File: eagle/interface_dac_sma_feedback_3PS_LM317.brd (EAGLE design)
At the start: 95.6 x 144.9 mm, 38 parts, among them IC1 ISO1540, X1 BU-SMA-V

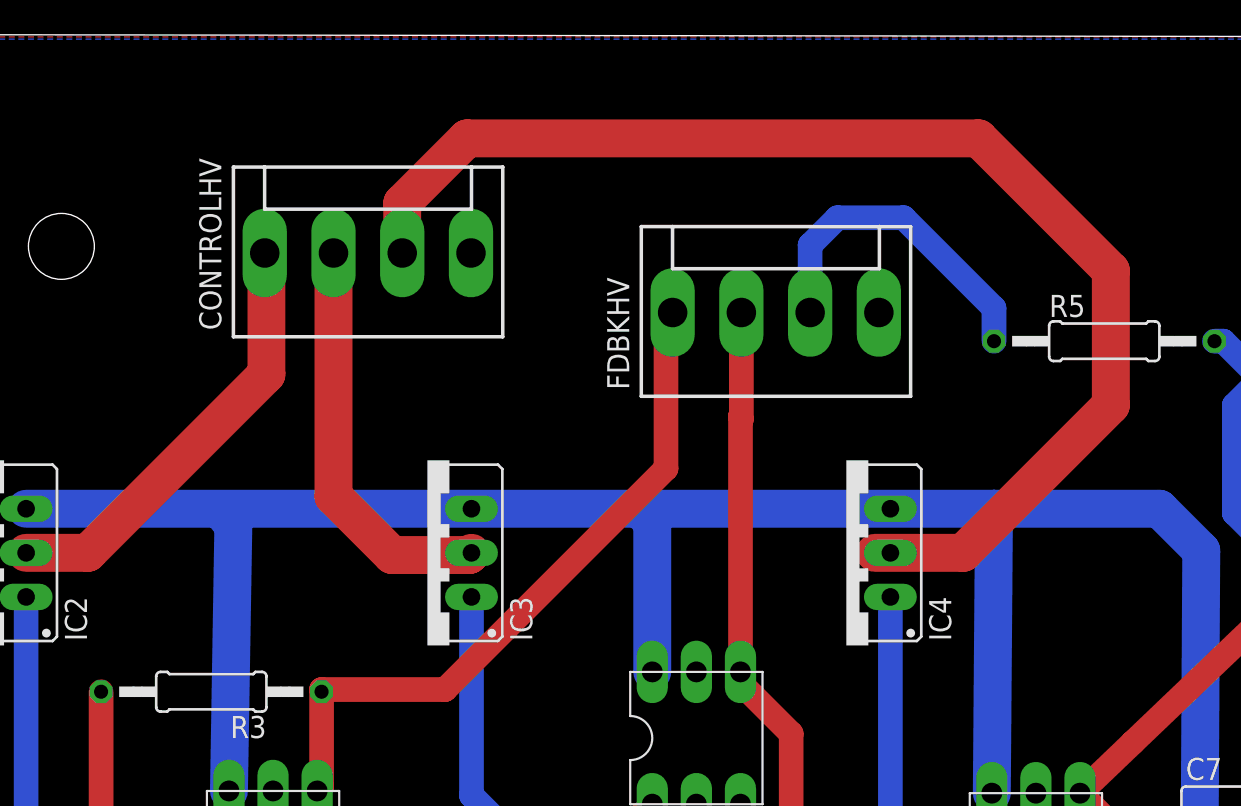
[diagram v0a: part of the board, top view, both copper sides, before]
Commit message: ultra layout. try that next time with lm317 interface
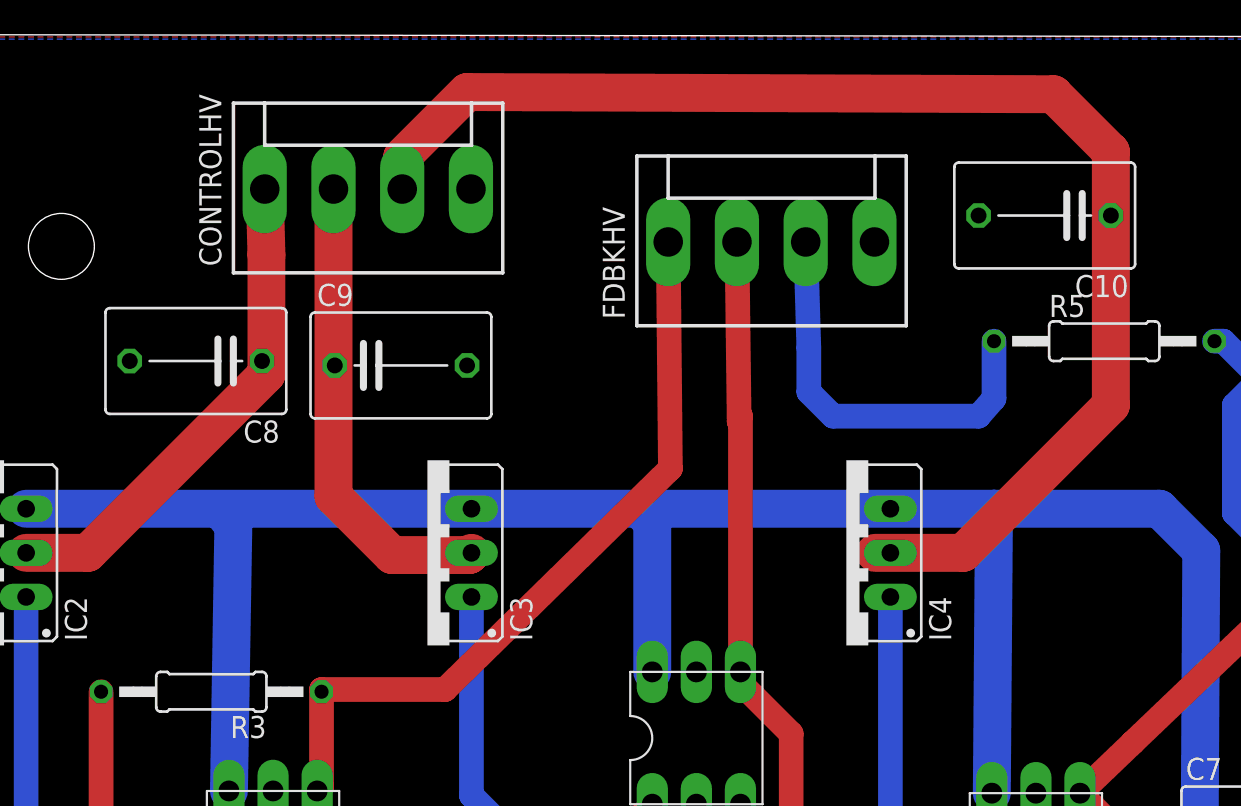
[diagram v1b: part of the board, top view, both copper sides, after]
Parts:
- added C10, C8, C9: (no value), resistor:C075-063X106
- moved FDBKHV 4.07 mm to (47.4, 133.0)
- moved CONTROLHV 3.68 mm to (24.1, 136.0)
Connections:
- net GND: now also C10.2, C8.2, C9.2
- net N$11: now also C9.1
- net N$4: now also C8.1
- net N$5: now also C10.1
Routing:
- net N$9: track 19.2 -> 23.6 mm
- net N$6: track 36.0 -> 40.4 mm
- net N$5: track 73.3 -> 77.3 mm
- net N$8: track 40.3 -> 44.3 mm
- net N$11: track 23.4 -> 27.1 mm
- net N$4: track 25.1 -> 28.8 mm
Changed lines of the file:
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@@
 <attribute name="OC_FARNELL" value="unknown" x="13.335" y="45.212" size="1.778" layer="27" display="off"/>
 </element>
-<element name="CONTROLHV" library="con-molex" package="KK-156-4" value="" x="24.13" y="132.334">
-<attribute name="OC_NEWARK" value="unknown" x="24.13" y="132.334" size="1.778" layer="27" display="off"/>
-<attribute name="MPN" value="" x="24.13" y="132.334" size="1.778" layer="27" display="off"/>
-<attribute name="MF" value="" x="24.13" y="132.334" size="1.778" layer="27" display="off"/>
-<attribute name="OC_FARNELL" value="unknown" x="24.13" y="132.334" size="1.778" layer="27" display="off"/>
+<element name="CONTROLHV" library="con-molex" package="KK-156-4" value="" x="24.13" y="136.017">
+<attribute name="OC_NEWARK" value="unknown" x="24.13" y="136.017" size="1.778" layer="27" display="off"/>
+<attribute name="MPN" value="" x="24.13" y="136.017" size="1.778" layer="27" display="off"/>
+<attribute name="MF" value="" x="24.13" y="136.017" size="1.778" layer="27" display="off"/>
+<attribute name="OC_FARNELL" value="unknown" x="24.13" y="136.017" size="1.778" layer="27" display="off"/>
 </element>
-<element name="FDBKHV" library="con-molex" package="KK-156-4" value="40k" x="47.625" y="128.905">
-<attribute name="OC_NEWARK" value="unknown" x="47.625" y="128.905" size="1.778" layer="27" display="off"/>
-<attribute name="MPN" value="" x="47.625" y="128.905" size="1.778" layer="27" display="off"/>
-<attribute name="MF" value="" x="47.625" y="128.905" size="1.778" layer="27" display="off"/>
-<attribute name="OC_FARNELL" value="unknown" x="47.625" y="128.905" size="1.778" layer="27" display="off"/>
+<element name="FDBKHV" library="con-molex" package="KK-156-4" value="40k" x="47.371" y="132.969">
+<attribute name="OC_NEWARK" value="unknown" x="47.371" y="132.969" size="1.778" layer="27" display="off"/>
+<attribute name="MPN" value="" x="47.371" y="132.969" size="1.778" layer="27" display="off"/>
+<attribute name="MF" value="" x="47.371" y="132.969" size="1.778" layer="27" display="off"/>
+<attribute name="OC_FARNELL" value="unknown" x="47.371" y="132.969" size="1.778" layer="27" display="off"/>
 </element>
 <element name="POWERINTERFACE" library="con-molex" package="KK-156-4" value="" x="84.074" y="89.027">
@@
 <element name="R11" library="resistor" package="0207/12" value="20k" x="36.068" y="88.519"/>
 <element name="R12" library="resistor" package="0207/12" value="12" x="56.769" y="83.947"/>
+<element name="C8" library="resistor" package="C075-063X106" value="" x="14.224" y="126.111" rot="R180"/>
+<element name="C9" library="resistor" package="C075-063X106" value="" x="26.035" y="125.857"/>
+<element name="C10" library="resistor" package="C075-063X106" value="" x="63.119" y="134.493" rot="R180"/>
 </elements>
 <signals>
@@
 </polygon>
 <contactref element="C7" pad="2"/>
+<contactref element="C8" pad="2"/>
+<contactref element="C9" pad="2"/>
+<contactref element="C10" pad="2"/>
 </signal>
 <signal name="PWM6">
@@
 <contactref element="FDBKHV" pad="1"/>
 <contactref element="U$6" pad="P$4"/>
-<wire x1="41.304" y1="128.778" x2="41.685" y2="128.905" width="1.4224" layer="1"/>
 <contactref element="R3" pad="1"/>
-<wire x1="41.304" y1="128.778" x2="41.304" y2="119.917" width="1.4224" layer="1"/>
-<wire x1="41.304" y1="119.917" x2="28.575" y2="107.188" width="1.4224" layer="1"/>
+<wire x1="41.431" y1="132.969" x2="41.558" y2="119.917" width="1.4224" layer="1"/>
+<wire x1="41.558" y1="119.917" x2="28.575" y2="107.188" width="1.4224" layer="1"/>
 <wire x1="28.575" y1="107.188" x2="21.463" y2="107.188" width="1.4224" layer="1"/>
 <wire x1="21.463" y1="107.188" x2="21.463" y2="101.6" width="1.4224" layer="1"/>
@@
 <wire x1="8.001" y1="115.062" x2="18.288" y2="125.349" width="2.1844" layer="1"/>
 <wire x1="18.288" y1="125.349" x2="18.288" y2="132.236" width="2.1844" layer="1"/>
-<wire x1="18.288" y1="132.236" x2="18.19" y2="132.334" width="2.1844" layer="1"/>
+<wire x1="18.288" y1="132.236" x2="18.19" y2="136.017" width="2.1844" layer="1"/>
+<contactref element="C8" pad="1"/>
+<wire x1="18.288" y1="125.349" x2="18.034" y2="126.111" width="0" layer="19" extent="1-1"/>
 </signal>
 <signal name="N$5">
 <contactref element="CONTROLHV" pad="3"/>
 <contactref element="IC4" pad="2"/>
-<wire x1="26.11" y1="132.334" x2="26.11" y2="135.203" width="2.1844" layer="1"/>
-<wire x1="26.11" y1="135.203" x2="29.845" y2="138.938" width="2.1844" layer="1"/>
-<wire x1="29.845" y1="138.938" x2="59.309" y2="138.938" width="2.1844" layer="1"/>
-<wire x1="59.309" y1="138.938" x2="66.929" y2="131.318" width="2.1844" layer="1"/>
-<wire x1="66.929" y1="131.318" x2="66.929" y2="123.571" width="2.1844" layer="1"/>
+<wire x1="26.11" y1="136.017" x2="26.11" y2="137.87" width="2.1844" layer="1"/>
+<wire x1="26.11" y1="137.87" x2="29.845" y2="141.605" width="2.1844" layer="1"/>
+<wire x1="29.845" y1="141.605" x2="63.627" y2="141.478" width="2.1844" layer="1"/>
+<wire x1="63.627" y1="141.478" x2="66.929" y2="138.176" width="2.1844" layer="1"/>
+<wire x1="66.929" y1="138.176" x2="66.929" y2="123.571" width="2.1844" layer="1"/>
 <wire x1="66.929" y1="123.571" x2="58.42" y2="115.062" width="2.1844" layer="1"/>
 <wire x1="58.42" y1="115.062" x2="53.34" y2="115.062" width="2.1844" layer="1"/>
-<wire x1="53.34" y1="115.062" x2="54.229" y2="115.062" width="0" layer="19" extent="1-1"/>
+<contactref element="C10" pad="1"/>
+<wire x1="66.929" y1="138.176" x2="66.929" y2="134.493" width="0" layer="19" extent="1-1"/>
+<wire x1="54.229" y1="115.062" x2="53.34" y2="115.062" width="0" layer="19" extent="1-1"/>
 </signal>
 <signal name="N$6">
 <contactref element="FDBKHV" pad="2"/>
 <contactref element="U$5" pad="P$4"/>
-<wire x1="45.645" y1="128.905" x2="45.645" y2="122.757" width="1.4224" layer="1"/>
-<wire x1="45.645" y1="122.757" x2="45.593" y2="122.936" width="1.4224" layer="1"/>
+<wire x1="45.391" y1="132.969" x2="45.518" y2="122.63" width="1.4224" layer="1"/>
+<wire x1="45.518" y1="122.63" x2="45.593" y2="122.936" width="1.4224" layer="1"/>
 <wire x1="45.593" y1="122.936" x2="45.593" y2="108.204" width="1.4224" layer="1"/>
 <contactref element="R4" pad="1"/>
@@
 <contactref element="CONTROLHV" pad="2"/>
 <contactref element="IC3" pad="2"/>
-<wire x1="22.15" y1="132.334" x2="22.15" y2="118.312" width="2.1844" layer="1"/>
+<wire x1="22.15" y1="136.017" x2="22.15" y2="118.312" width="2.1844" layer="1"/>
 <wire x1="22.15" y1="118.312" x2="25.527" y2="114.935" width="2.1844" layer="1"/>
 <wire x1="25.527" y1="114.935" x2="29.972" y2="114.935" width="2.1844" layer="1"/>
 <wire x1="29.972" y1="114.935" x2="30.099" y2="115.062" width="2.1844" layer="1"/>
+<contactref element="C9" pad="1"/>
+<wire x1="22.15" y1="118.312" x2="22.225" y2="125.857" width="0" layer="19" extent="1-1"/>
 </signal>
 <signal name="-5V">
@@
 <contactref element="R5" pad="1"/>
 <contactref element="FDBKHV" pad="3"/>
-<wire x1="49.605" y1="128.905" x2="49.605" y2="132.79" width="1.4224" layer="16"/>
-<wire x1="49.605" y1="132.79" x2="51.181" y2="134.366" width="1.4224" layer="16"/>
-<wire x1="51.181" y1="134.366" x2="54.991" y2="134.366" width="1.4224" layer="16"/>
-<wire x1="54.991" y1="134.366" x2="60.198" y2="129.159" width="1.4224" layer="16"/>
-<wire x1="60.198" y1="129.159" x2="60.198" y2="127.254" width="1.4224" layer="16"/>
+<wire x1="49.351" y1="132.969" x2="49.53" y2="126.873" width="1.4224" layer="16"/>
+<wire x1="49.53" y1="126.873" x2="49.53" y2="124.333" width="1.4224" layer="16"/>
+<wire x1="49.53" y1="124.333" x2="50.927" y2="122.936" width="1.4224" layer="16"/>
+<wire x1="50.927" y1="122.936" x2="59.309" y2="122.936" width="1.4224" layer="16"/>
+<wire x1="59.309" y1="122.936" x2="60.198" y2="123.952" width="1.4224" layer="16"/>
+<wire x1="60.198" y1="123.952" x2="60.198" y2="127.254" width="1.4224" layer="16"/>
 </signal>
 <signal name="N$23">

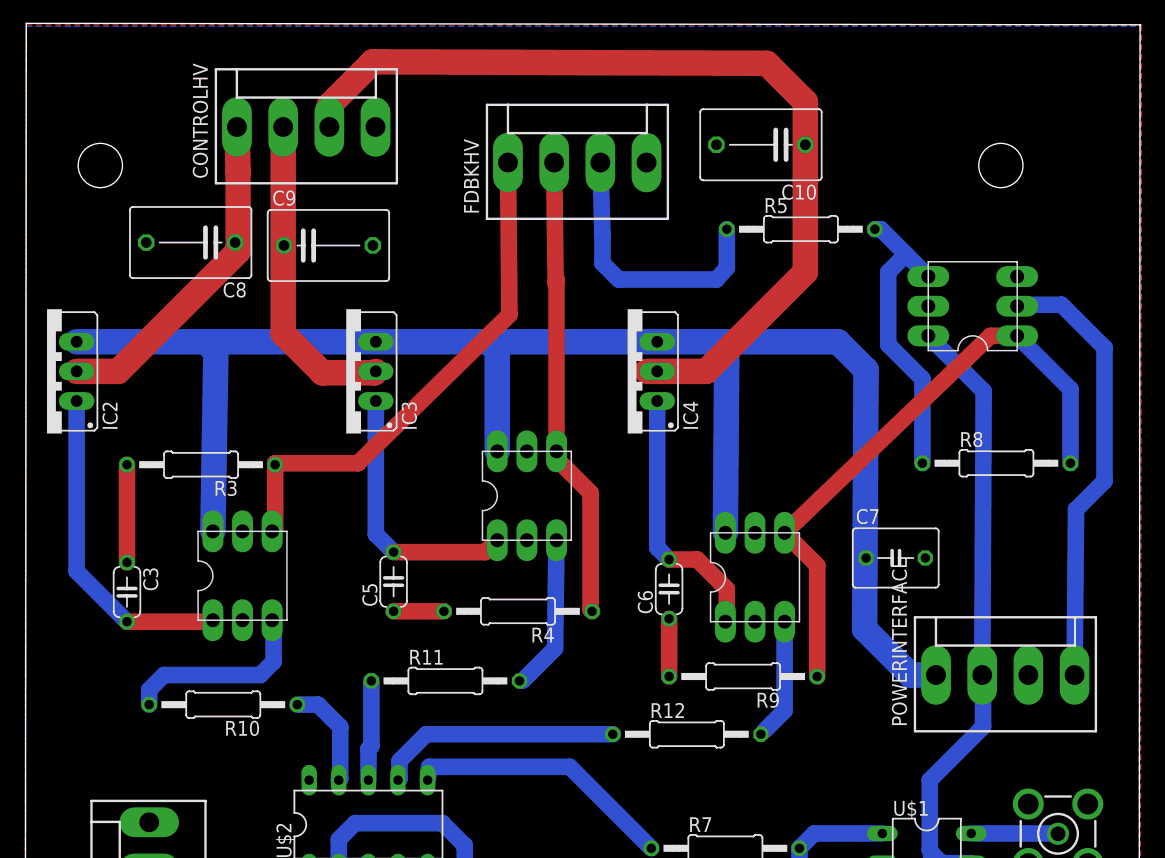
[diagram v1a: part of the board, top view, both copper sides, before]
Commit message: Fix negative rail problems
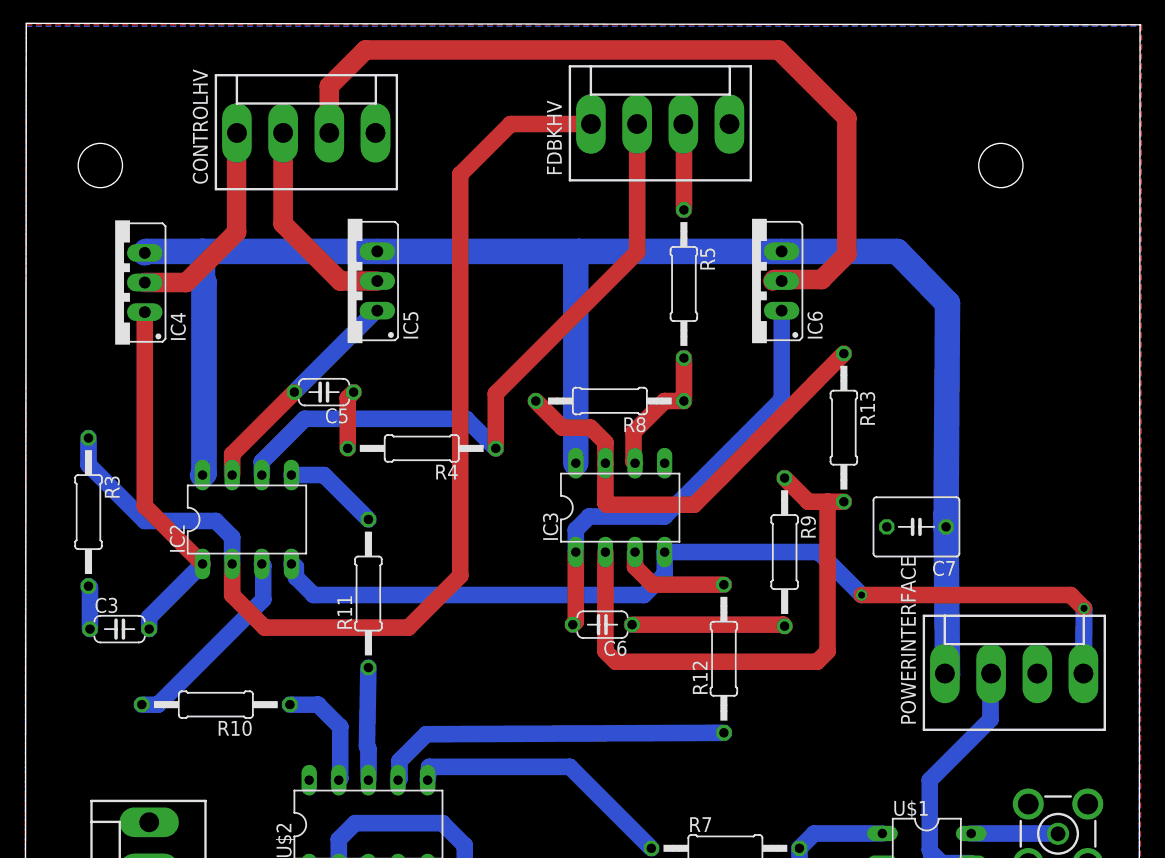
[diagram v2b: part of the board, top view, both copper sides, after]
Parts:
- removed C10, C8, C9: (no value), resistor:C075-063X106
- removed U$3, U$4, U$5, U$6: OPA735DIL, texas:DIL6
- added IC5, IC6: (no value), v-reg:317TS
- added R13: 10k, resistor:0207/12
- C3, C4, C5, C6, C7: value (none) -> 10n
- FDBKHV: value 40k -> (none)
- IC2, IC3: value (none) -> LT1352PA; device v-reg:317TS -> linear-technology:DIL08
- R10, R11: value 20k -> 10k
- R3, R4, R9: value (none) -> 10k
- moved IC4 44.6 mm to (7.75, 122.7)
- moved R8 33.6 mm to (50.2, 112.5), turned to 180 degrees
- moved IC3 26.2 mm to (51.1, 103.4), turned to 0 degrees
- moved IC2 21.3 mm to (19.1, 102.4), turned to 0 degrees
- moved C5 17.3 mm to (25.7, 113.3), turned to 180 degrees
- moved R4 16.2 mm to (34.0, 108.5)
- moved R9 11.2 mm to (65.2, 99.6), turned to 270 degrees
- moved R5 11.1 mm to (56.5, 122.6), turned to 270 degrees
- moved R3 10.5 mm to (5.46, 103.0), turned to 270 degrees
- moved R11 9.99 mm to (29.5, 96.0), turned to 90 degrees
- moved FDBKHV 7.84 mm to (54.5, 136.3)
- moved R12 7.21 mm to (59.9, 90.4), turned to 90 degrees
- moved C6 6.48 mm to (49.5, 93.3), turned to 180 degrees
- moved C3 3.24 mm to (8.13, 93.0), turned to 0 degrees
- moved C7 3.21 mm to (76.5, 101.7), turned to 180 degrees
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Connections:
- new net N$27: IC3.2, R13.2, R9.1
- net +12V: now also IC2.8, IC3.8, IC5.3, IC6.3; no longer IC2.3, IC3.3, U$4.P$6, U$5.P$6, U$6.P$6
- net -5V: now also IC2.4, IC3.4; no longer U$3.P$2
- net GND: now also IC3.5; no longer C10.2, C8.2, C9.2, U$3.P$3, U$4.P$2, U$5.P$2, U$6.P$2
- net N$10: now also IC2.7, IC5.1; no longer IC3.1, U$5.P$1
- net N$11: now also CONTROLHV.3, IC6.2; no longer C9.1, CONTROLHV.2, IC3.2
- net N$14: now also IC3.7, R13.1; no longer R9.1, U$3.P$1, U$4.P$4
- net N$16: now also IC2.3; no longer U$6.P$3
- net N$17: now also IC2.5; no longer U$5.P$3
- net N$18: now also IC3.3; no longer U$4.P$3
- net N$19: now also IC4.1; no longer U$6.P$1
- net N$21: now also IC3.1, IC6.1; no longer IC4.1, U$4.P$1
- net N$23: now also IC3.6; no longer U$3.P$4
- net N$4: now also IC4.2; no longer C8.1, IC2.2
- net N$5: now also CONTROLHV.2, IC5.2; no longer C10.1, CONTROLHV.3, IC4.2
- net N$6: now also IC2.6; no longer U$5.P$4
- net N$8: now also IC2.2; no longer U$6.P$4
- net VCC: no longer U$3.P$6
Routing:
- net N$5: track 77.3 -> 17.9 mm
- net N$8: track 44.3 -> 92.1 mm
- net -5V: track 38.2 -> 85.4 mm, vias 0 -> 2
- net N$27: track 0.00 -> 47.0 mm
- net N$11: track 27.1 -> 71.1 mm
- net VCC: track 160.2 -> 130.4 mm
- net N$9: track 23.6 -> 7.39 mm
- net N$6: track 40.4 -> 56.6 mm
- net N$21: track 22.9 -> 38.6 mm
- net N$14: track 53.0 -> 38.6 mm
- net N$23: track 26.0 -> 11.8 mm
- net N$4: track 28.8 -> 18.5 mm
- net N$25: track 20.9 -> 30.5 mm
- net N$20: track 4.95 -> 13.1 mm
- net N$17: track 13.2 -> 8.18 mm
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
